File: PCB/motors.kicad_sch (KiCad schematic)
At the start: 17 parts, among them J10 DOOR_LCK, J12 WIN_SW, J2 OUT_WIN, J5 OUT_DOOR, SW1 DOOR_LCK, SW3 WIN_SW, U4 MAX22201ATC+

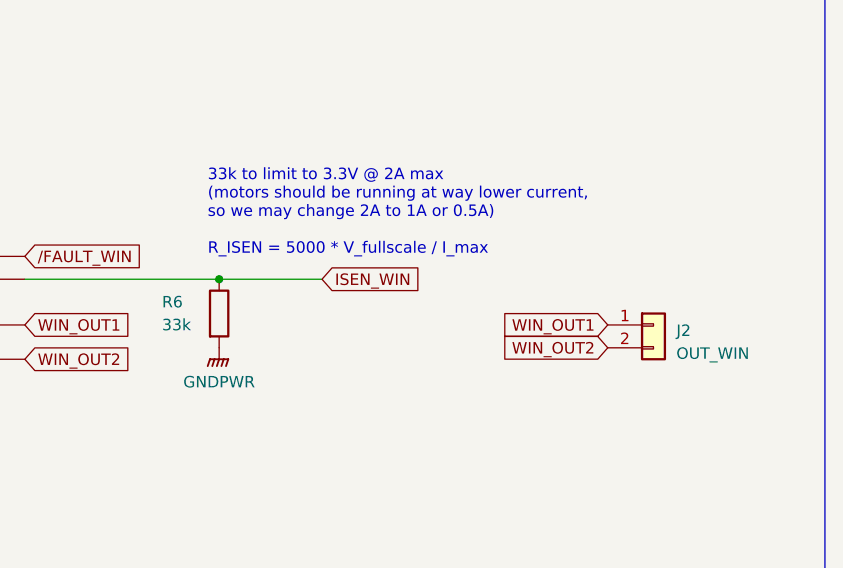
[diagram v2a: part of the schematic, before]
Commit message: added all components
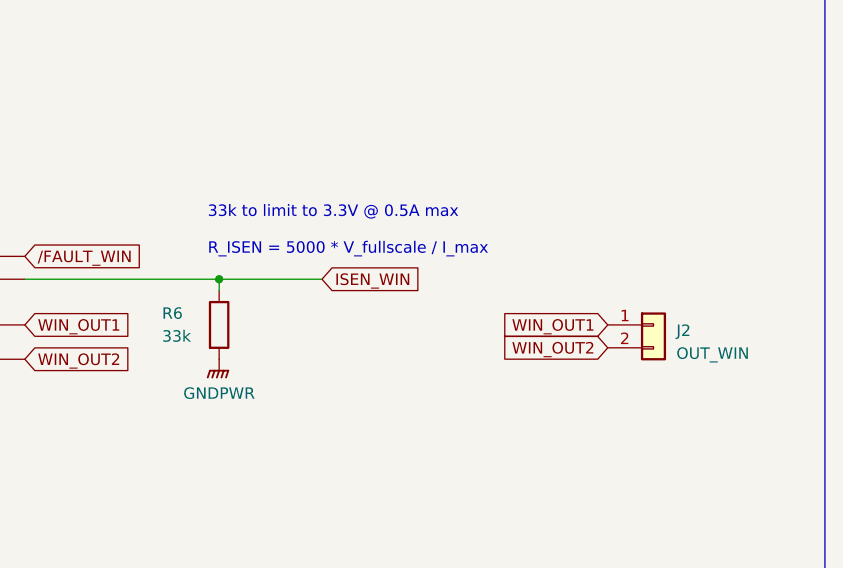
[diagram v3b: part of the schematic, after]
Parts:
- C22, C24, C25, C26: footprint (none) -> Capacitor_SMD:C_0805_2012Metric
- C23, C27: footprint (none) -> Capacitor_THT:CP_Radial_D5.0mm_P2.00mm
- J10, J2, J5: footprint (none) -> TerminalBlock_MetzConnect:TerminalBlock_MetzConnect_Type011_RT05502HBWC_1x02_P5.00mm_Horizontal
- J12: footprint (none) -> TerminalBlock_MetzConnect:TerminalBlock_MetzConnect_Type011_RT05504HBWC_1x04_P5.00mm_Horizontal
- R5, R6, R7: footprint (none) -> Resistor_SMD:R_0805_2012Metric
- SW1: footprint (none) -> Button_Switch_THT:SW_CW_GPTS203211B
- SW3: footprint (none) -> Button_Switch_SMD:SW_DIP_SPSTx04_Slide_6.7x11.72mm_W8.61mm_P2.54mm_LowProfile
- U4: footprint (none) -> kicad_models:MAX22201ATC_
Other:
- note added: "33k to limit to 3.3V @ 0.5A max R_ISEN = 5000 * V_fullscale / I_max"
- note removed: "33k to limit to 3.3V @ 2A max (motors should be running at way lower current, so we may change 2A to 1A or 0.5A) R_ISEN = 5000 * V_fullscale / I_max"
- moved on the sheet: R6
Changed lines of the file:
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@@
+    (stroke (width 0) (type default))
+  )
+  (wire (pts (xy 132.08 55.88) (xy 132.08 54.61))
     (stroke (width 0) (type default))
   )
@@
     (effects (font (size 4 4)) (justify left bottom))
   )
-  (text "33k to limit to 3.3V @ 2A max \n(motors should be running at way lower current,\nso we may change 2A to 1A or 0.5A)\n\nR_ISEN = 5000 * V_fullscale / I_max"
+  (text "33k to limit to 3.3V @ 0.5A max \n\nR_ISEN = 5000 * V_fullscale / I_max"
     (at 130.81 52.07 0)
     (effects (font (size 1.27 1.27)) (justify left bottom))
@@
       (effects (font (size 1.27 1.27)) (justify left))
     )
-    (property "Footprint" "" (at 29.21 50.8 0)
+    (property "Footprint" "TerminalBlock_MetzConnect:TerminalBlock_MetzConnect_Type011_RT05504HBWC_1x04_P5.00mm_Horizontal" (at 29.21 50.8 0)
       (effects (font (size 1.27 1.27)) hide)
     )
@@
       (effects (font (size 1.27 1.27)) (justify left))
     )
-    (property "Footprint" "" (at 180.34 59.69 0)
+    (property "Footprint" "TerminalBlock_MetzConnect:TerminalBlock_MetzConnect_Type011_RT05502HBWC_1x02_P5.00mm_Horizontal" (at 180.34 59.69 0)
       (effects (font (size 1.27 1.27)) hide)
     )
@@
       (effects (font (size 1.27 1.27)) (justify left))
     )
-    (property "Footprint" "" (at 35.56 144.78 0)
+    (property "Footprint" "TerminalBlock_MetzConnect:TerminalBlock_MetzConnect_Type011_RT05502HBWC_1x02_P5.00mm_Horizontal" (at 35.56 144.78 0)
       (effects (font (size 1.27 1.27)) hide)
     )
@@
       (effects (font (size 1.27 1.27)))
     )
-    (property "Footprint" "" (at 31.75 76.2 0)
+    (property "Footprint" "Button_Switch_SMD:SW_DIP_SPSTx04_Slide_6.7x11.72mm_W8.61mm_P2.54mm_LowProfile" (at 31.75 76.2 0)
       (effects (font (size 1.27 1.27)) hide)
     )
@@
       (effects (font (size 1.27 1.27)) (justify left))
     )
-    (property "Footprint" "" (at 87.3252 181.61 0)
+    (property "Footprint" "Capacitor_SMD:C_0805_2012Metric" (at 87.3252 181.61 0)
       (effects (font (size 1.27 1.27)) hide)
     )
@@
       (effects (font (size 1.27 1.27)) (justify left))
     )
-    (property "Footprint" "" (at 74.422 85.09 90)
+    (property "Footprint" "Resistor_SMD:R_0805_2012Metric" (at 74.422 85.09 90)
       (effects (font (size 1.27 1.27)) hide)
     )
@@
       (effects (font (size 1.27 1.27)) (justify left))
     )
-    (property "Footprint" "" (at 105.1052 129.54 0)
+    (property "Footprint" "Capacitor_THT:CP_Radial_D5.0mm_P2.00mm" (at 105.1052 129.54 0)
       (effects (font (size 1.27 1.27)) hide)
     )
@@
       (effects (font (size 1.27 1.27)) (justify left))
     )
-    (property "Footprint" "" (at 88.5952 36.83 0)
+    (property "Footprint" "Capacitor_SMD:C_0805_2012Metric" (at 88.5952 36.83 0)
       (effects (font (size 1.27 1.27)) hide)
     )
@@
       (effects (font (size 1.27 1.27)) (justify left))
     )
-    (property "Footprint" "" (at 93.6752 129.54 0)
+    (property "Footprint" "Capacitor_SMD:C_0805_2012Metric" (at 93.6752 129.54 0)
       (effects (font (size 1.27 1.27)) hide)
     )
@@
       (effects (font (size 1.27 1.27)) (justify left))
     )
-    (property "Footprint" "" (at 79.502 177.8 90)
+    (property "Footprint" "Resistor_SMD:R_0805_2012Metric" (at 79.502 177.8 90)
       (effects (font (size 1.27 1.27)) hide)
     )
@@
       (effects (font (size 1.27 1.27)) (justify left))
     )
-    (property "Footprint" "" (at 158.75 151.13 0)
+    (property "Footprint" "TerminalBlock_MetzConnect:TerminalBlock_MetzConnect_Type011_RT05502HBWC_1x02_P5.00mm_Horizontal" (at 158.75 151.13 0)
       (effects (font (size 1.27 1.27)) hide)
     )
@@
       (effects (font (size 1.524 1.524)))
     )
-    (property "Footprint" "" (at 69.85 146.05 0)
+    (property "Footprint" "kicad_models:MAX22201ATC_" (at 69.85 146.05 0)
       (effects (font (size 1.27 1.27) italic) hide)
     )
@@
       (effects (font (size 1.27 1.27)) (justify left))
     )
-    (property "Footprint" "" (at 82.2452 88.9 0)
+    (property "Footprint" "Capacitor_SMD:C_0805_2012Metric" (at 82.2452 88.9 0)
       (effects (font (size 1.27 1.27)) hide)
     )
@@
       (effects (font (size 1.27 1.27)))
     )
-    (property "Footprint" "" (at 35.56 156.21 0)
+    (property "Footprint" "Button_Switch_THT:SW_CW_GPTS203211B" (at 35.56 156.21 0)
       (effects (font (size 1.27 1.27)) hide)
     )
@@
       (effects (font (size 1.27 1.27)) (justify left))
     )
-    (property "Footprint" "" (at 100.0252 36.83 0)
+    (property "Footprint" "Capacitor_THT:CP_Radial_D5.0mm_P2.00mm" (at 100.0252 36.83 0)
       (effects (font (size 1.27 1.27)) hide)
     )
@@
       (effects (font (size 1.524 1.524)))
     )
-    (property "Footprint" "" (at 64.77 53.34 0)
+    (property "Footprint" "kicad_models:MAX22201ATC_" (at 64.77 53.34 0)
       (effects (font (size 1.27 1.27) italic) hide)
     )
@@
     )
   )
-  (symbol (lib_id "power:GNDPWR") (at 132.08 62.23 0) (unit 1)
-    (in_bom yes) (on_board yes) (dnp no)
-    (property "Reference" "#PWR035" (at 132.08 67.31 0)
-      (effects (font (size 1.27 1.27)) hide)
-    )
-    (property "Value" "GNDPWR" (at 132.08 66.04 0)
-      (effects (font (size 1.27 1.27)))
-    )
-    (property "Footprint" "" (at 132.08 63.5 0)
-      (effects (font (size 1.27 1.27)) hide)
-    )
-    (property "Datasheet" "" (at 132.08 63.5 0)
+  (symbol (lib_id "power:GNDPWR") (at 132.08 63.5 0) (unit 1)
+    (in_bom yes) (on_board yes) (dnp no)
+    (property "Reference" "#PWR035" (at 132.08 68.58 0)
+      (effects (font (size 1.27 1.27)) hide)
+    )
+    (property "Value" "GNDPWR" (at 132.08 67.31 0)
+      (effects (font (size 1.27 1.27)))
+    )
+    (property "Footprint" "" (at 132.08 64.77 0)
+      (effects (font (size 1.27 1.27)) hide)
+    )
+    (property "Datasheet" "" (at 132.08 64.77 0)
       (effects (font (size 1.27 1.27)) hide)
     )
@@
     )
   )
-  (symbol (lib_id "Device:R") (at 132.08 58.42 0) (unit 1)
-    (in_bom yes) (on_board yes) (dnp no)
-    (property "Reference" "R6" (at 125.73 57.15 0)
-      (effects (font (size 1.27 1.27)) (justify left))
-    )
-    (property "Value" "33k" (at 125.73 59.69 0)
-      (effects (font (size 1.27 1.27)) (justify left))
-    )
-    (property "Footprint" "" (at 130.302 58.42 90)
-      (effects (font (size 1.27 1.27)) hide)
-    )
-    (property "Datasheet" "~" (at 132.08 58.42 0)
-      (effects (font (size 1.27 1.27)) hide)
-    )
+  (symbol (lib_id "Device:R") (at 132.08 59.69 0) (unit 1)
+    (in_bom yes) (on_board yes) (dnp no)
+    (property "Reference" "R6" (at 125.73 58.42 0)
+      (effects (font (size 1.27 1.27)) (justify left))
+    )
+    (property "Value" "33k" (at 125.73 60.96 0)
+      (effects (font (size 1.27 1.27)) (justify left))
+    )
+    (property "Footprint" "Resistor_SMD:R_0805_2012Metric" (at 130.302 59.69 90)
+      (effects (font (size 1.27 1.27)) hide)
+    )
+    (property "Datasheet" "~" (at 132.08 59.69 0)
+      (effects (font (size 1.27 1.27)) hide)
+    )

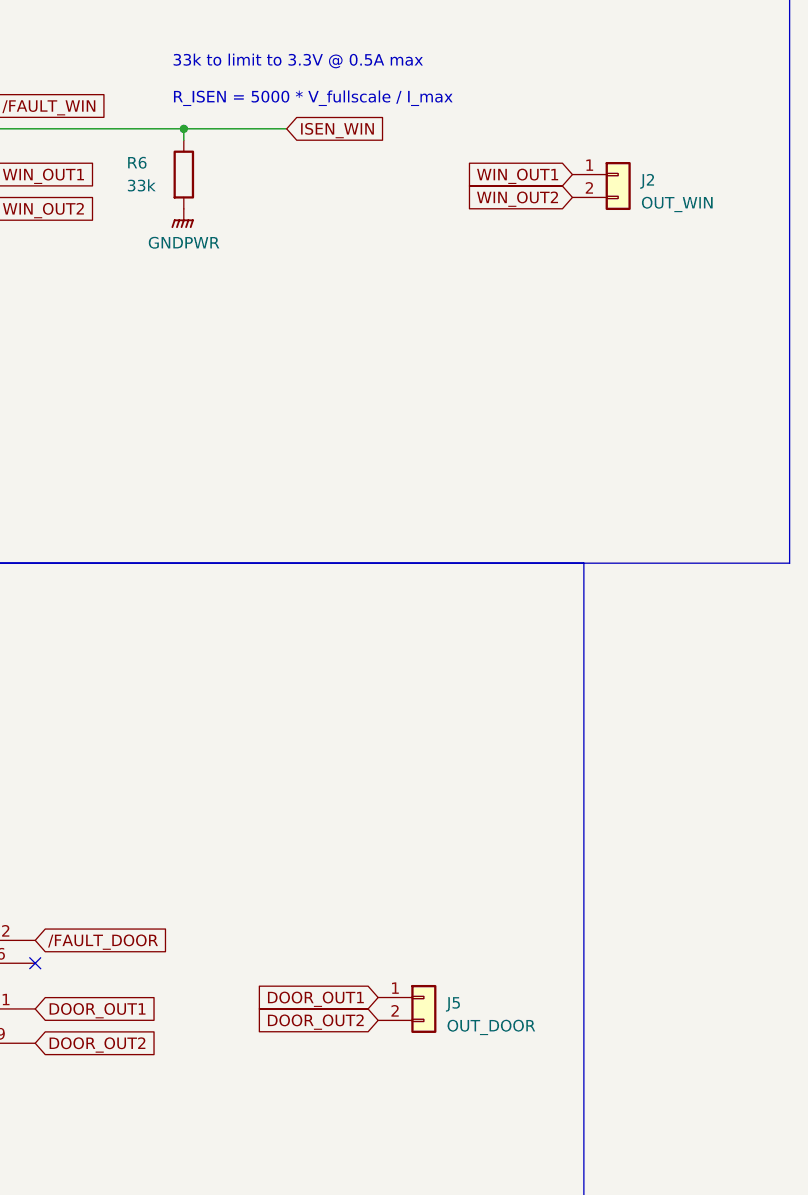
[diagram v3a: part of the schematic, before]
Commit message: canvis a sortides de potencia
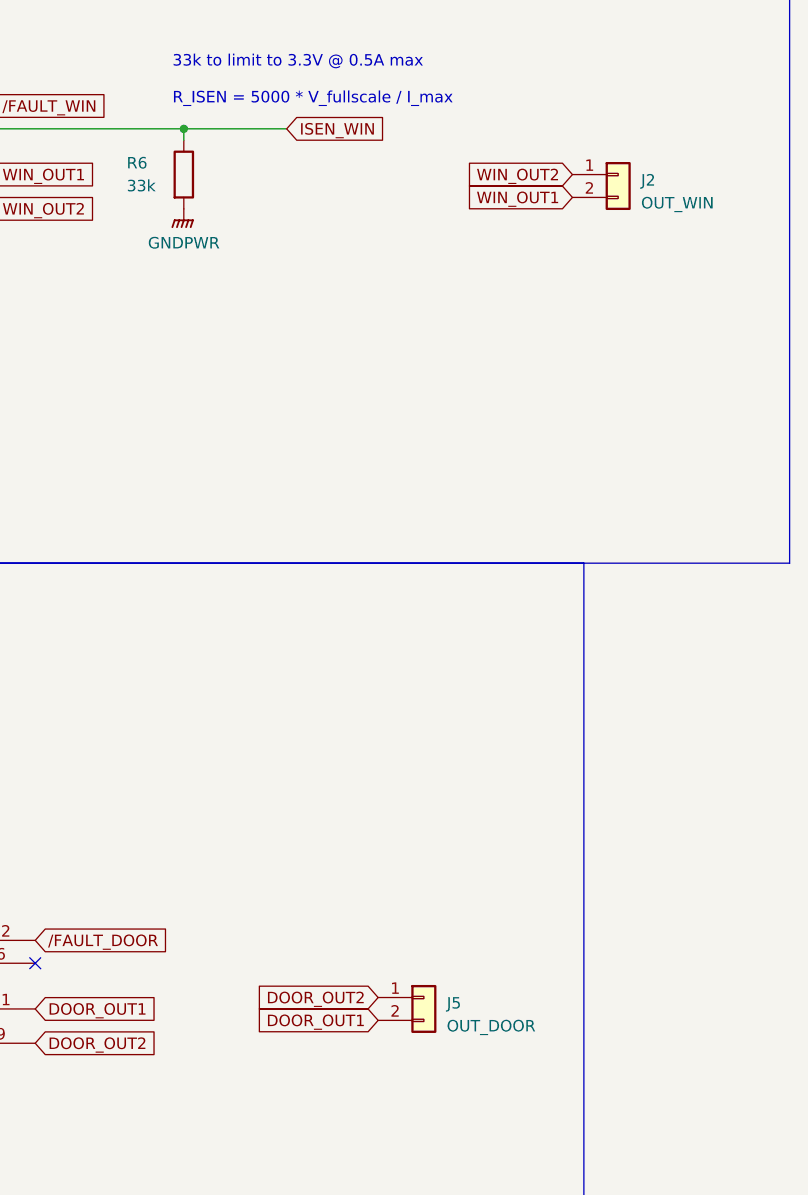
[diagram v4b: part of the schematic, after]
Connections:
- net DOOR_OUT1: now also J5.2 (Pin_2); no longer J5.1 (Pin_1)
- net DOOR_OUT2: now also J5.1 (Pin_1); no longer J5.2 (Pin_2)
- net WIN_OUT1: now also J2.2 (Pin_2); no longer J2.1 (Pin_1)
- net WIN_OUT2: now also J2.1 (Pin_1); no longer J2.2 (Pin_2)
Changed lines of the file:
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@@
     (effects (font (size 1.27 1.27)) (justify left bottom))
+  )
+  (global_label "DOOR_OUT1" (shape input) (at 153.67 153.67 180) (fields_autoplaced)
+    (effects (font (size 1.27 1.27)) (justify right))
+    (property "Intersheetrefs" "${INTERSHEET_REFS}" (at 139.7575 153.67 0)
+      (effects (font (size 1.27 1.27)) (justify right) hide)
+    )
   )
   (global_label "DOOR_OUT1" (shape input) (at 115.57 152.4 0) (fields_autoplaced)
@@
     (effects (font (size 1.27 1.27)) (justify right))
     (property "Intersheetrefs" "${INTERSHEET_REFS}" (at 57.6308 152.4 0)
-      (effects (font (size 1.27 1.27)) (justify right) hide)
-    )
-  )
-  (global_label "DOOR_OUT1" (shape input) (at 153.67 151.13 180) (fields_autoplaced)
-    (effects (font (size 1.27 1.27)) (justify right))
-    (property "Intersheetrefs" "${INTERSHEET_REFS}" (at 139.7575 151.13 0)
       (effects (font (size 1.27 1.27)) (justify right) hide)
     )
@@
     )
   )
-  (global_label "WIN_OUT2" (shape input) (at 175.26 62.23 180) (fields_autoplaced)
+  (global_label "WIN_OUT2" (shape input) (at 175.26 59.69 180) (fields_autoplaced)
     (effects (font (size 1.27 1.27)) (justify right))
-    (property "Intersheetrefs" "${INTERSHEET_REFS}" (at 163.1618 62.23 0)
+    (property "Intersheetrefs" "${INTERSHEET_REFS}" (at 163.1618 59.69 0)
       (effects (font (size 1.27 1.27)) (justify right) hide)
     )
@@
     )
   )
-  (global_label "WIN_OUT1" (shape input) (at 175.26 59.69 180) (fields_autoplaced)
+  (global_label "WIN_OUT1" (shape input) (at 175.26 62.23 180) (fields_autoplaced)
     (effects (font (size 1.27 1.27)) (justify right))
-    (property "Intersheetrefs" "${INTERSHEET_REFS}" (at 163.1618 59.69 0)
+    (property "Intersheetrefs" "${INTERSHEET_REFS}" (at 163.1618 62.23 0)
       (effects (font (size 1.27 1.27)) (justify right) hide)
     )
@@
     )
   )
-  (global_label "DOOR_OUT2" (shape input) (at 153.67 153.67 180) (fields_autoplaced)
+  (global_label "DOOR_OUT2" (shape input) (at 153.67 151.13 180) (fields_autoplaced)
     (effects (font (size 1.27 1.27)) (justify right))
-    (property "Intersheetrefs" "${INTERSHEET_REFS}" (at 139.7575 153.67 0)
+    (property "Intersheetrefs" "${INTERSHEET_REFS}" (at 139.7575 151.13 0)
       (effects (font (size 1.27 1.27)) (justify right) hide)
     )

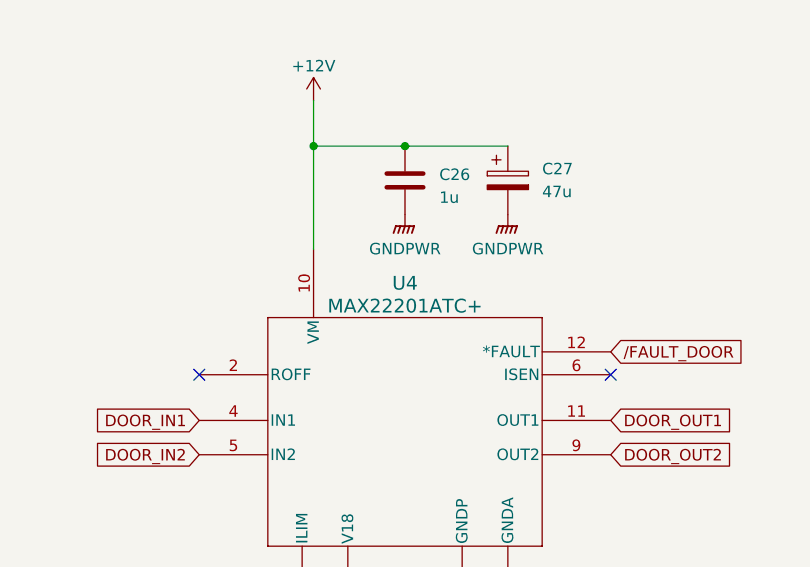
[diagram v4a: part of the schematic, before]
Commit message: netclasses esquematic
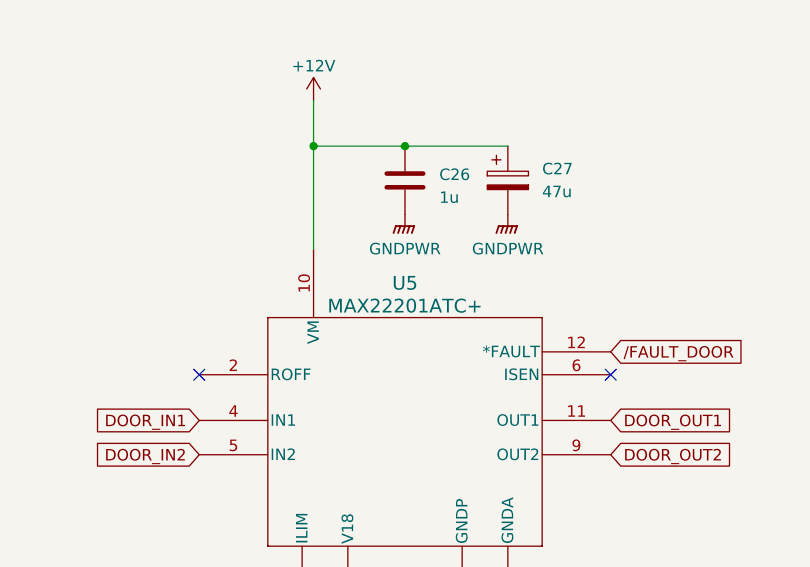
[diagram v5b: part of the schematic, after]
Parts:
- renumbered U4 to U5
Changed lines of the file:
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@@
   (symbol (lib_id "MAX22201ATC_:MAX22201ATC+") (at 69.85 146.05 0) (unit 1)
     (in_bom yes) (on_board yes) (dnp no) (fields_autoplaced)
-    (property "Reference" "U4" (at 92.71 137.16 0)
+    (property "Reference" "U5" (at 92.71 137.16 0)
       (effects (font (size 1.524 1.524)))
     )
@@
     (instances
       (project "DIJOUS_4_PORTES"
-        (path "/69b34976-047e-478e-bd76-9b6ef0dba356/6b83d062-cc2b-4223-9dc9-bddc64623104"
-          (reference "U4") (unit 1)
-        )
         (path "/69b34976-047e-478e-bd76-9b6ef0dba356/1c250547-8c37-4478-9ce5-99247889367f"
           (reference "U5") (unit 1)
@@
     (instances
       (project "DIJOUS_4_PORTES"
-        (path "/69b34976-047e-478e-bd76-9b6ef0dba356/6b83d062-cc2b-4223-9dc9-bddc64623104"
-          (reference "U4") (unit 1)
-        )
         (path "/69b34976-047e-478e-bd76-9b6ef0dba356/1c250547-8c37-4478-9ce5-99247889367f"
           (reference "U4") (unit 1)

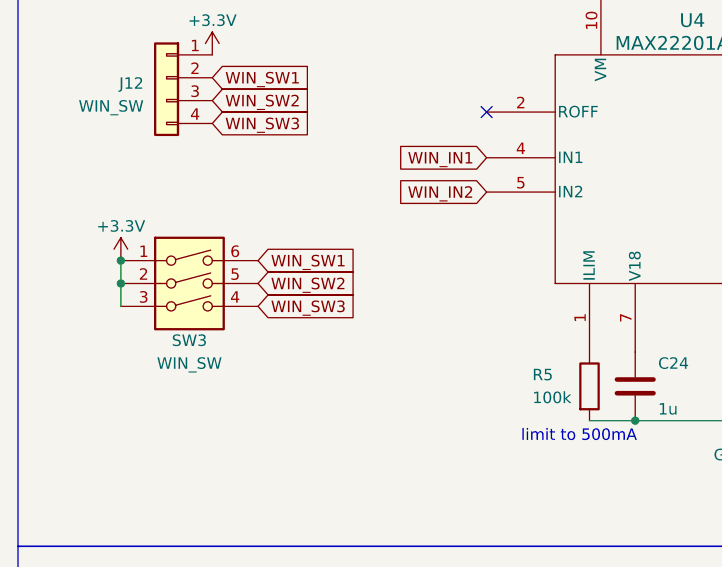
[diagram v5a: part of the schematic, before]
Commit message: first PCB done, need to correct vias and solve all DRC errors
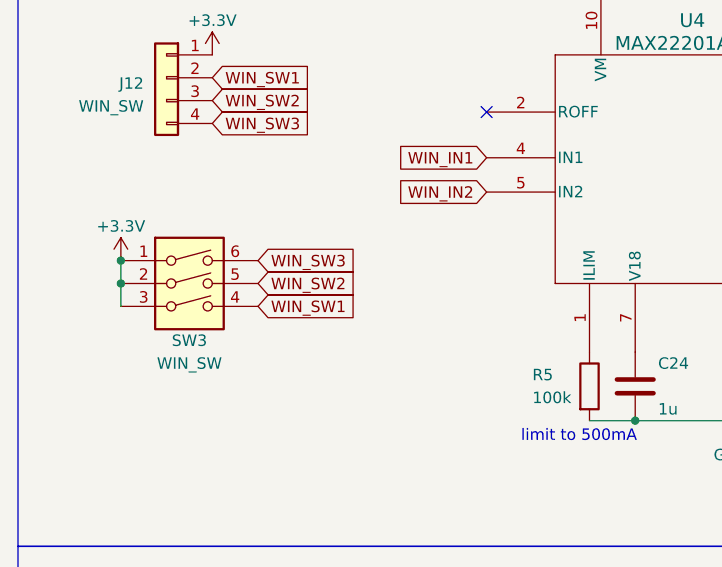
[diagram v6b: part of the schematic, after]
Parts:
- SW3: footprint Button_Switch_SMD:SW_DIP_SPSTx04_Slide_6.7x11.72mm_W8.61mm_P2.54mm_LowProfile -> Button_Switch_SMD:SW_DIP_SPSTx03_Slide_6.7x9.18mm_W8.61mm_P2.54mm_LowProfile
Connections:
- net WIN_SW1: now also SW3.4; no longer SW3.6
- net WIN_SW3: now also SW3.6; no longer SW3.4
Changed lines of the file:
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@@
     )
   )
-  (global_label "WIN_SW3" (shape input) (at 39.37 76.2 0) (fields_autoplaced)
+  (global_label "WIN_SW3" (shape input) (at 39.37 71.12 0) (fields_autoplaced)
     (effects (font (size 1.27 1.27)) (justify left))
-    (property "Intersheetrefs" "${INTERSHEET_REFS}" (at 50.5005 76.2 0)
+    (property "Intersheetrefs" "${INTERSHEET_REFS}" (at 50.5005 71.12 0)
       (effects (font (size 1.27 1.27)) (justify left) hide)
     )
@@
     )
   )
-  (global_label "WIN_SW1" (shape input) (at 39.37 71.12 0) (fields_autoplaced)
+  (global_label "WIN_SW1" (shape input) (at 39.37 76.2 0) (fields_autoplaced)
     (effects (font (size 1.27 1.27)) (justify left))
-    (property "Intersheetrefs" "${INTERSHEET_REFS}" (at 50.5799 71.12 0)
+    (property "Intersheetrefs" "${INTERSHEET_REFS}" (at 50.5799 76.2 0)
       (effects (font (size 1.27 1.27)) (justify left) hide)
     )
@@
       (effects (font (size 1.27 1.27)))
     )
-    (property "Footprint" "Button_Switch_SMD:SW_DIP_SPSTx04_Slide_6.7x11.72mm_W8.61mm_P2.54mm_LowProfile" (at 31.75 76.2 0)
+    (property "Footprint" "Button_Switch_SMD:SW_DIP_SPSTx03_Slide_6.7x9.18mm_W8.61mm_P2.54mm_LowProfile" (at 31.75 76.2 0)
       (effects (font (size 1.27 1.27)) hide)
     )
